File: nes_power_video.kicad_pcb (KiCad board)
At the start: 2 copper layers, 59.9 x 59.7 mm, 13 parts, among them J2 Audio, J3 Video, J4 Conn_01x05, Q1 2SA1015

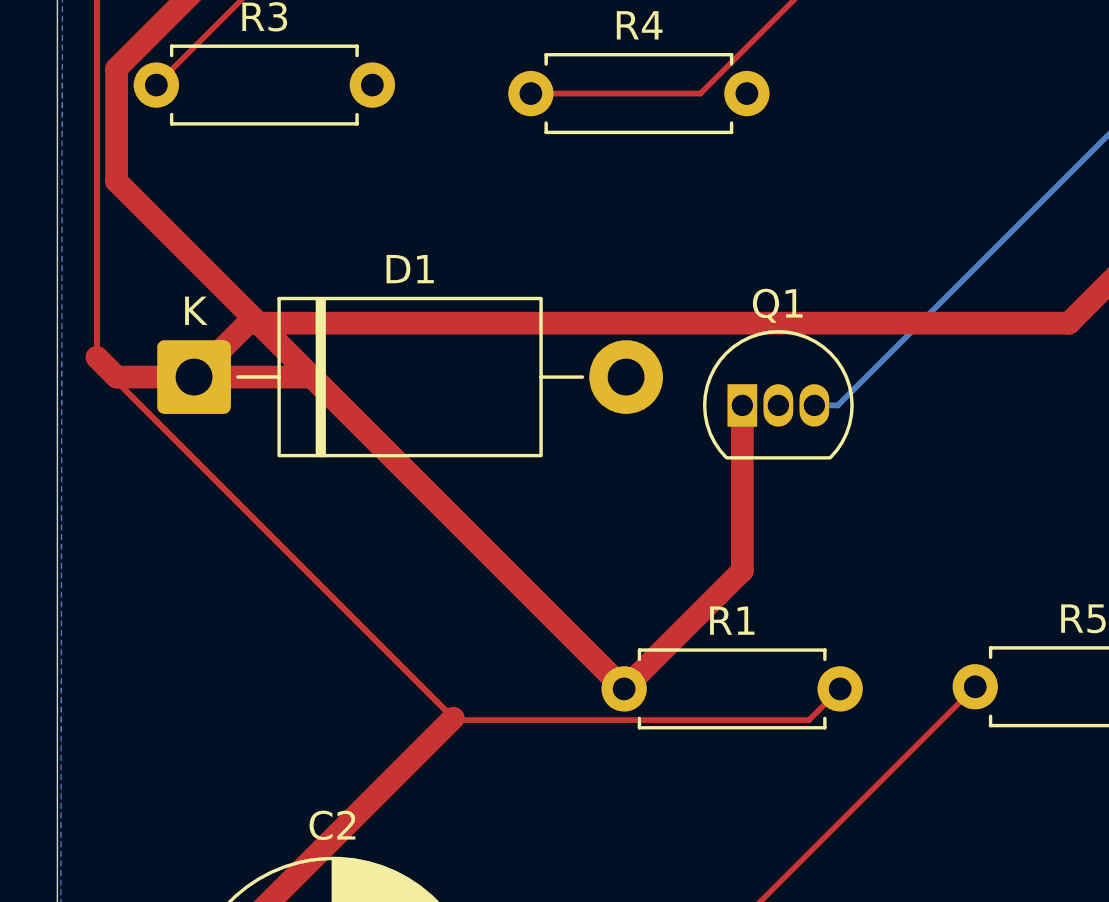
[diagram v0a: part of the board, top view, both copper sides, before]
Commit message: Fix Q1 emitter node shorted to +5V rail (breaks video output)
R1 had both terminals on the /5V net, so Q1's emitter was clamped to the
rail and C2 coupled +5V rather than video into R5/J3. The composite
output could never have worked, on any v1 board.

Root cause: an R2 (110 ohm) sat between /5V and the emitter node until
2026-07-04. When it was deleted, KiCad merged its two leftover collinear
wire stubs into a single wire from (24.13,129.54) to (24.13,194.31),
welding the emitter node onto /5V and shorting R1 across it. Confirmed by
exporting netlists across the KiCad auto-backups: last good at 21:17:29,
broken at 22:15:13 the same evening.

Schematic: removed that wire plus the six-segment /5V run that existed
only to feed R2's top pin, and the junction dot left mid-wire. Netlist is
now /5V = C1.1 D1.1 F1.1 J4.3 R1.2 and Net-(Q1-E) = C2.1 Q1.1 R1.1, which
matches the last-good topology with R1 alone as the 300 ohm emitter load.
ERC is unchanged at 10 pre-existing warnings.

PCB: split the emitter node out of the /5V pour. Dropped the two traces
tying R1 pad 1 to the rail and the C2 branch that ran to R1 pad 2, moved
the C2 branch onto R1 pad 1, re-netted the Q1/C2 segments to Net-(Q1-E),
and routed R1 pad 2 to the rail down the clear corridor at x=47.5. Added
a short link restoring the F1 branch, which the deletions had otherwise
orphaned. DRC is identical to baseline: 2 pre-existing violations, 0
unconnected.

Chose R1 alone over restoring the R2 divider: in an emitter follower the
base sets the operating point, so the divider's shunt leg only burns
~6.5mA and drops the AC load from 100 to 52 ohms. R1 alone also matches
the BOM and needs no new footprint.

README documents the defect and the cut-and-verify rework for assembled
v1 boards.

Co-Authored-By: Claude Opus 5 <noreply@anthropic.com>
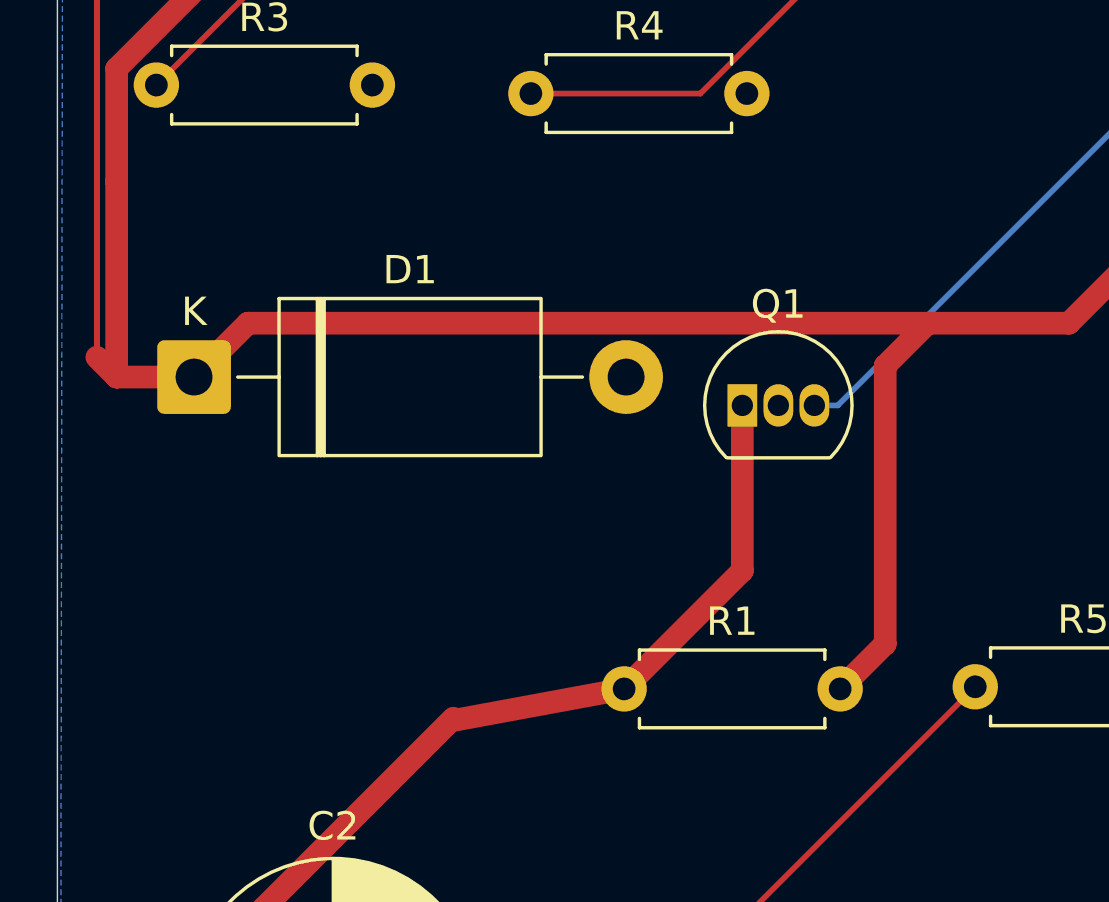
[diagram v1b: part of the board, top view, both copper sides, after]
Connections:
- C2 pad 1: /5V -> Net-(Q1-E)
- Q1 pad 1: /5V -> Net-(Q1-E)
- R1 pad 1: /5V -> Net-(Q1-E)
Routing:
- net /5V: track 238.6 -> 140.3 mm
- net Net-(Q1-E): track 0.00 -> 30.7 mm
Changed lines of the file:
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@@
 			(layers "*.Cu" "*.Mask")
 			(remove_unused_layers no)
-			(net "/5V")
+			(net "Net-(Q1-E)")
 			(pintype "passive")
 		)
@@
 			(layers "*.Cu" "*.Mask")
 			(remove_unused_layers no)
-			(net "/5V")
+			(net "Net-(Q1-E)")
 			(pinfunction "E_1")
 			(pintype "passive")
@@
 			(remove_unused_layers no)
 			(roundrect_rratio 0.125)
-			(net "/5V")
+			(net "Net-(Q1-E)")
 			(pintype "passive")
 		)
@@
 	)
 	(segment
-		(start 27.29 45)
-		(end 38.29 56)
-		(width 0.8)
-		(layer "F.Cu")
-		(net "/5V")
-	)
-	(segment
 		(start 25.02 43.1)
 		(end 53.98 43.1)
@@
 	)
 	(segment
-		(start 44.81 57.1)
-		(end 45.91 56)
-		(width 0.2)
-		(layer "F.Cu")
-		(net "/5V")
-	)
-	(segment
 		(start 20.39 34.1201)
 		(end 20.39 38.1)
@@
 		(width 0.8)
 		(layer "F.Cu")
-		(net "/5V")
-	)
-	(segment
-		(start 19.69 44.4547)
-		(end 32.3353 57.1)
-		(width 0.2)
-		(layer "F.Cu")
-		(net "/5V")
+		(net "Net-(Q1-E)")
 	)
 	(segment
@@
 		(width 0.8)
 		(layer "F.Cu")
-		(net "/5V")
+		(net "Net-(Q1-E)")
 	)
 	(segment
@@
 	)
 	(segment
-		(start 23.12 45)
-		(end 27.29 45)
-		(width 0.8)
-		(layer "F.Cu")
-		(net "/5V")
-	)
-	(segment
 		(start 32.26765 57.03235)
 		(end 32.3353 57.1)
 		(width 0.2)
 		(layer "F.Cu")
-		(net "/5V")
+		(net "Net-(Q1-E)")
 	)
 	(segment
@@
 		(width 0.8)
 		(layer "F.Cu")
-		(net "/5V")
-	)
-	(segment
-		(start 32.3353 57.1)
-		(end 44.81 57.1)
-		(width 0.2)
-		(layer "F.Cu")
-		(net "/5V")
+		(net "Net-(Q1-E)")
 	)
 	(segment
@@
 		(width 0.8)
 		(layer "F.Cu")
-		(net "/5V")
-	)
-	(segment
-		(start 20.39 38.1)
-		(end 38.29 56)
-		(width 0.8)
-		(layer "F.Cu")
-		(net "/5V")
-	)
-	(segment
-		(start 19.69 44.4547)
-		(end 32.26765 57.03235)
-		(width 0.2)
-		(layer "F.Cu")
-		(net "/5V")
+		(net "Net-(Q1-E)")
 	)
 	(segment
@@
 		(net "Net-(J3-TIP)")
 	)
+	(segment
+		(start 32.3353 57.1)
+		(end 38.29 56)
+		(width 0.8)
+		(layer "F.Cu")
+		(net "Net-(Q1-E)")
+	)
+	(segment
+		(start 20.39 38.1)
+		(end 20.39 45)
+		(width 0.8)
+		(layer "F.Cu")
+		(net "/5V")
+	)
+	(segment
+		(start 45.91 56)
+		(end 47.5 54.41)
+		(width 0.8)
+		(layer "F.Cu")
+		(net "/5V")
+	)
+	(segment
+		(start 47.5 54.41)
+		(end 47.5 44.6)
+		(width 0.8)
+		(layer "F.Cu")
+		(net "/5V")
+	)
+	(segment
+		(start 47.5 44.6)
+		(end 49 43.1)
+		(width 0.8)
+		(layer "F.Cu")
+		(net "/5V")
+	)
 	(zone

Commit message: Add TPS2553 eFuse for real overcurrent protection
F1 (RHEF200, 2.0A hold / 3.8A trip) was the only overcurrent protection.
On a console drawing roughly 0.5-0.7A a 3.8A trip point protects nothing,
and a polyfuse takes seconds to act. U1 is now the real protection and F1
stays as a backup in case the eFuse fails short.

New power path:
  USB VBUS -> /raw_5v -> F1 -> /fused_5v -> U1 IN..OUT -> /5V -> load

U1 is a TI TPS2553DBVR adjustable current-limited switch in SOT-23-6:
resistor-programmed limit, ~3ms internal soft-start, thermal shutdown and
reverse-voltage protection. R6 = 22k sets a ~1.18A typical limit. Note the
relationship is inverse (I_OS ~ 25.9 / R_ILIM in kohm) - the datasheet spec
table gives 15k->1700mA, 20k->1295mA, 49.9k->520mA, 210k->130mA. C3 (100nF)
is U1's input decoupling, placed hard against pin 1 as TI requires.

EN is active-high on the TPS2553 and is tied to IN so the switch is always
on. FAULT is open-drain and left unconnected - nothing inside a closed NES
shell can read it. Ordered part is the plain TPS2553DBVR; the -1 suffix is
the latch-off variant, which would need a power cycle after each trip.

Pinout and the ILIM figures were taken from the TI datasheet rather than
from memory, which matters here: the pinout is IN/GND/EN/FAULT/ILIM/OUT
(pins 4 and 5 are easy to transpose) and an inverted reading of the ILIM
relationship would have produced a ~130mA limit that browns out the console.

Symbol: KiCad ships no TPS2553, so Custom.pretty/TPS2553DBV.kicad_sym adds
one, and a project sym-lib-table now registers it plus PJRAN1X1U03X so the
repo resolves its symbols without relying on a global table. Footprint is
the stock SOT-23-6_Handsoldering; R6/C3 are 0805 hand-solder.

PCB: U1, C3 and R6 sit in the band between R3 and D1 - the only pocket that
reaches F1's output, which the CC1/CC2 runs fence in on every other side.
The /5V spine is cut at (20.39,38.1)-(20.39,45) so F1 feeds U1's input, and
U1's output rejoins the spine. U1 is deliberat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
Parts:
- added C3: 100nF, Capacitor_SMD:C_0805_2012Metric_Pad1.18x1.45mm_HandSolder, F.Cu at (22.7, 39.1)
- added R6: 22k, Resistor_SMD:R_0805_2012Metric_Pad1.20x1.40mm_HandSolder, F.Cu at (33.0, 39.1)
- added U1: TPS2553DBV, Package_TO_SOT_SMD:SOT-23-6_Handsoldering, F.Cu at (27.8, 39.1)
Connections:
- F1 pad 1: /5V -> /fused_5v
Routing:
- net /fused_5v: track 0.00 -> 36.1 mm
- net /5V: track 140.3 -> 124.5 mm
- net GND: track 11.6 -> 15.4 mm, vias 4 -> 7
- net Net-(U1-ILIM): track 0.00 -> 2.85 mm

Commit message: Fix J3 video jack sleeve wired to the audio net instead of GND
The PJRAN1X1U03X swap in 73425bb landed existing wires on different
pins: Conn_Coaxial and PJRAN1X1U03X number and place their pins
differently, so J3 pin 1 (SLEEVE) ended up on Net-(J2-TIP) instead of
GND. That left the video jack's shell with no ground return and tied
the audio signal to it.

Schematic: drop J3.1 off the audio net and run it to the GND bus at
y=171.45.

PCB: delete the three B.Cu segments spurring off J2.2 to J3.1, re-net
J3 pad 1 to GND, and refill the B.Cu ground zone. J3 pad 1 is a
plated through-hole, so the back-layer ground pour now connects it
directly -- no extra routing needed.

ERC unchanged (10 warnings, all pre-existing). DRC unchanged
(2 violations, all pre-existing) with 0 unconnected items, and all 16
nets cross-check pin-for-pin between schematic and PCB.

The fabbed v1 board is not affected: its IPC netlist has J3.2 on GND.

Co-Authored-By: Claude Opus 5 <noreply@anthropic.com>
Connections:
- J3 pad 1: Net-(J2-TIP) -> GND
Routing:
- net Net-(J2-TIP): track 48.5 -> 16.4 mm

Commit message: Add bring-up test points for video, GND, +5V and audio
Four through-hole test points (TestPoint_THTPad_D2.0mm_Drill1.0mm), one
per signal the v2 bring-up needs to see:

  TP1 /VIDEO_OUT  (62.0, 60.0)    F.Cu stub to the existing R5->J3 run
  TP2 GND         (58.5, 60.0)    straight into the B.Cu pour
  TP3 /5V         (52.0, 43.1)    sits on the protected 5 V trunk
  TP4 /AUDIO_OUT  (65.9, 28.35)   B.Cu stub to the J4.2 -> J2 run

Also names the two signal nets. They were auto-generated Net-(J3-TIP)
and Net-(J2-TIP); labelling them /VIDEO_OUT and /AUDIO_OUT is what lets
the test points attach by label instead of by geometry, and makes the
netlist readable.

Placement notes: TP3 and TP4 both started in the corridor between J2 and
J4 and could not clear each other's courtyards, so TP3 moved onto the
wide /5V trunk near Q1. TP4 sits in the 1.2 mm-wide window between the
J4-Pin_1 diagonal and the /5V diagonal; do not nudge it without
re-running DRC.

Verified: ERC 10 warnings / 0 errors and DRC 2 violations / 0 unconnected
items, both identical to the pre-change baseline. All 16 nets cross-check
pin-for-pin between schematic and PCB.

Co-Authored-By: Claude Opus 5 <noreply@anthropic.com>
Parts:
- added TP1: VIDEO, TestPoint:TestPoint_THTPad_D2.0mm_Drill1.0mm, F.Cu at (62.0, 60.0)
- added TP2: GND, TestPoint:TestPoint_THTPad_D2.0mm_Drill1.0mm, F.Cu at (58.5, 60.0)
- added TP3: +5V, TestPoint:TestPoint_THTPad_D2.0mm_Drill1.0mm, F.Cu at (52.0, 43.1)
- added TP4: AUDIO, TestPoint:TestPoint_THTPad_D2.0mm_Drill1.0mm, F.Cu at (65.9, 28.4)
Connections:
- net Net-(J2-TIP) renamed /AUDIO_OUT
- net Net-(J3-TIP) renamed /VIDEO_OUT
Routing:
- net /VIDEO_OUT: track 18.2 -> 22.2 mm
- net /AUDIO_OUT: track 16.4 -> 19.4 mm

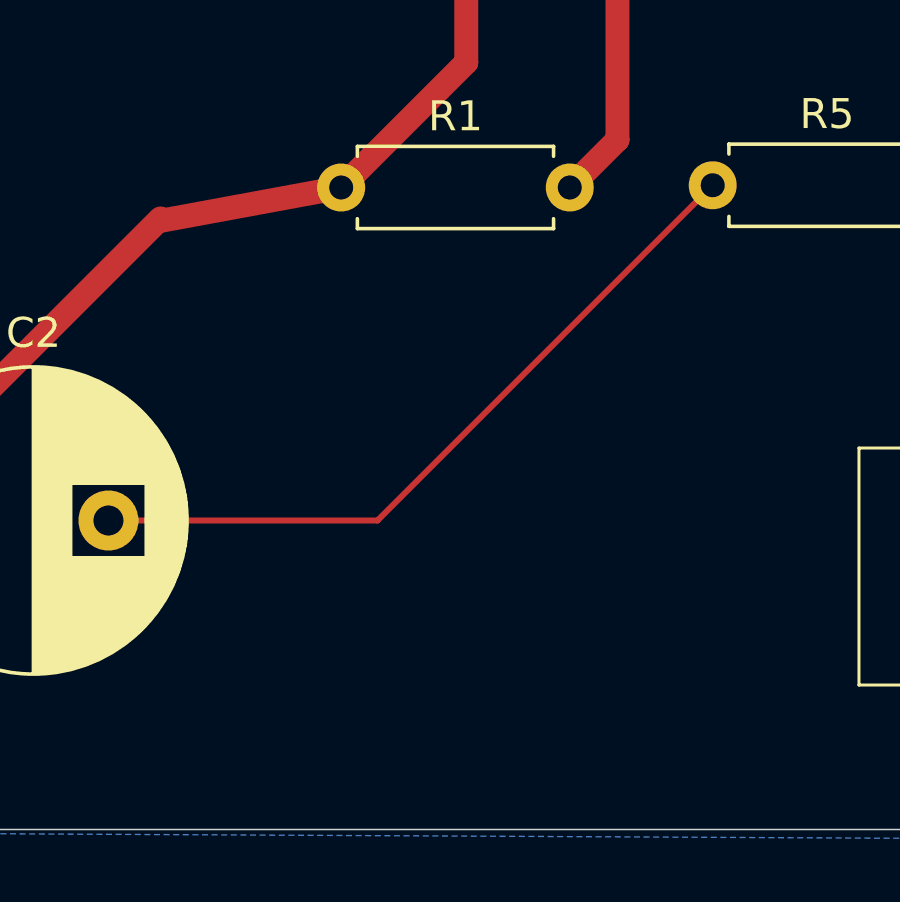
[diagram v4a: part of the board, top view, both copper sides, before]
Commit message: Add J5 feed header for the NESRGB 8-pin mini-DIN RGB connector
Provisions the Micomsoft XRGB-mini Framemeister connector standard that
the NESRGB board uses. The connector is NOT placed on this board: the
NESRGB kit ships it as a panel-mount jack that epoxies into a 12 mm hole
in the shell, so R/G/B run straight from the NESRGB to the connector and
this board only supplies the other three pins.

  J5.1 /RGB_VIDEO -> mini-DIN 3  composite video / sync, 75R
  J5.2 GND        -> mini-DIN 4
  J5.3 /5V        -> mini-DIN 5  (downstream of the TPS2553, so limited)

R7 (75 Ohm) is a second source termination off /VIDEO_BUF, mirroring R5.
Sharing R5 between the RCA jack and the mini-DIN would put two 75 Ohm
loads in parallel and halve the amplitude with both cables plugged in.

Also names the buffered video node: Net-(C2-Pad2) -> /VIDEO_BUF, so R7
can tap it by label.

Placement was constrained -- the Q1-E and VIDEO_BUF runs cut the lower
board in two on F.Cu, so J5's +5V leaves on B.Cu and vias up to R1.2.
J5 and R7 are placed from the libraries via pcbnew rather than embedded
by hand, which keeps them byte-identical to the library and avoids
lib_footprint_mismatch. The four test points also gained the
path/sheetname/sheetfile links they were missing, so a netlist re-import
will match them instead of duplicating them.

Caveat recorded in the README: two live outputs need R1 at 220 Ohm
rather than 330 Ohm, or the follower clips. Still unmeasured.

Verified: ERC 10 warnings / 0 errors and DRC 2 violations / 0 unconnected,
both identical to baseline. All 17 nets cross-check pin-for-pin.

Co-Authored-By: Claude Opus 5 <noreply@anthropic.com>
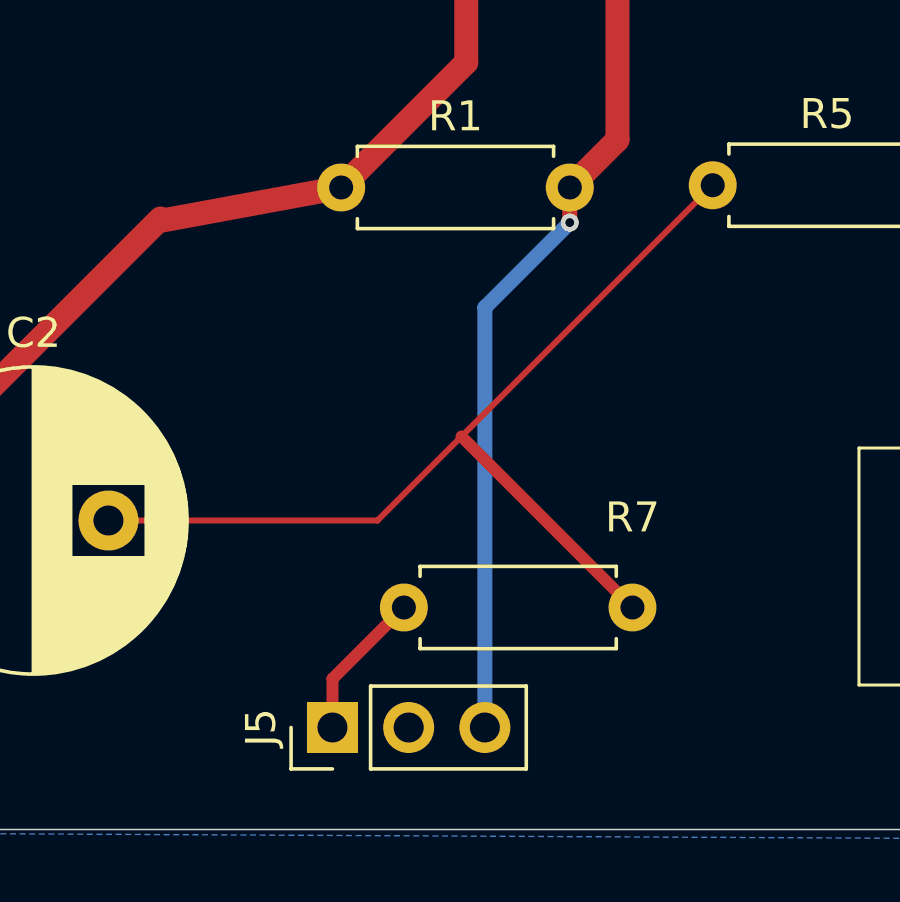
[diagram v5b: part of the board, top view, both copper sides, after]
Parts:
- added J5: RGB conn feed, PinHeader_1x03_P2.54mm_Vertical, F.Cu at (38.0, 74.0)
- added R7: 75 Ohm, R_Axial_DIN0207_L6.3mm_D2.5mm_P7.62mm_Horizontal, F.Cu at (48.0, 70.0)
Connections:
- net Net-(C2-Pad2) renamed /VIDEO_BUF
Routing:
- net /5V: track 124.5 -> 143.7 mm, vias 0 -> 1
- net /VIDEO_BUF: track 24.8 -> 32.8 mm
- net /RGB_VIDEO: track 0.00 -> 4.99 mm
